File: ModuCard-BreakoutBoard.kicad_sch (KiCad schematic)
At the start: 0 parts

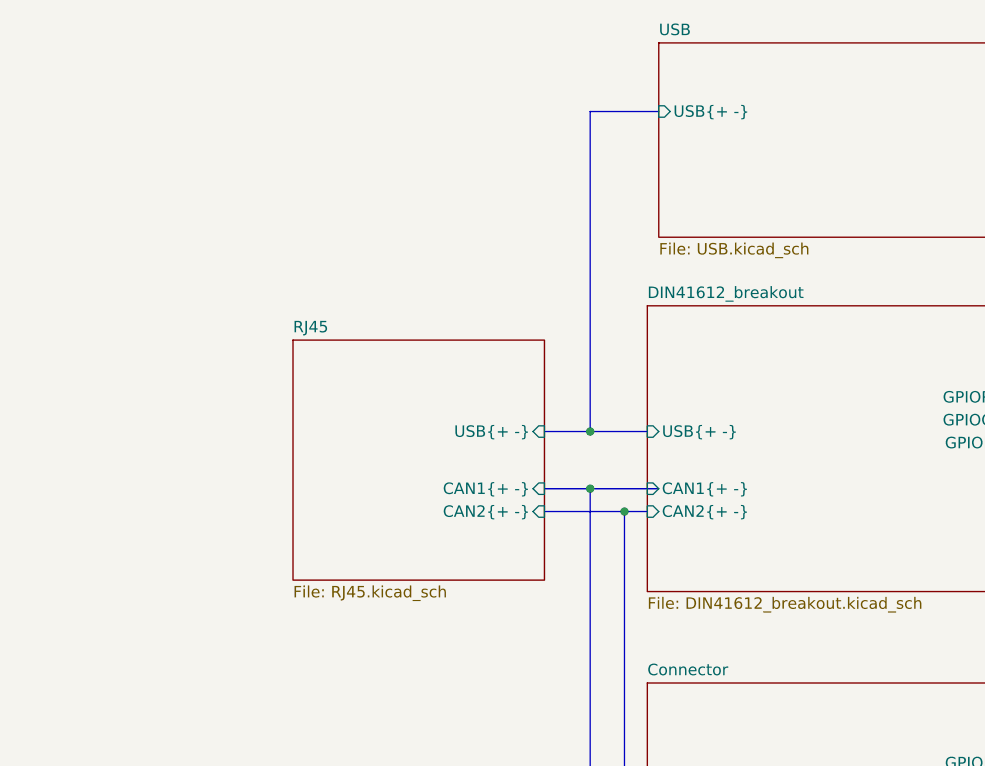
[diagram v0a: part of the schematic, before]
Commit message: Add multiplexer for USB
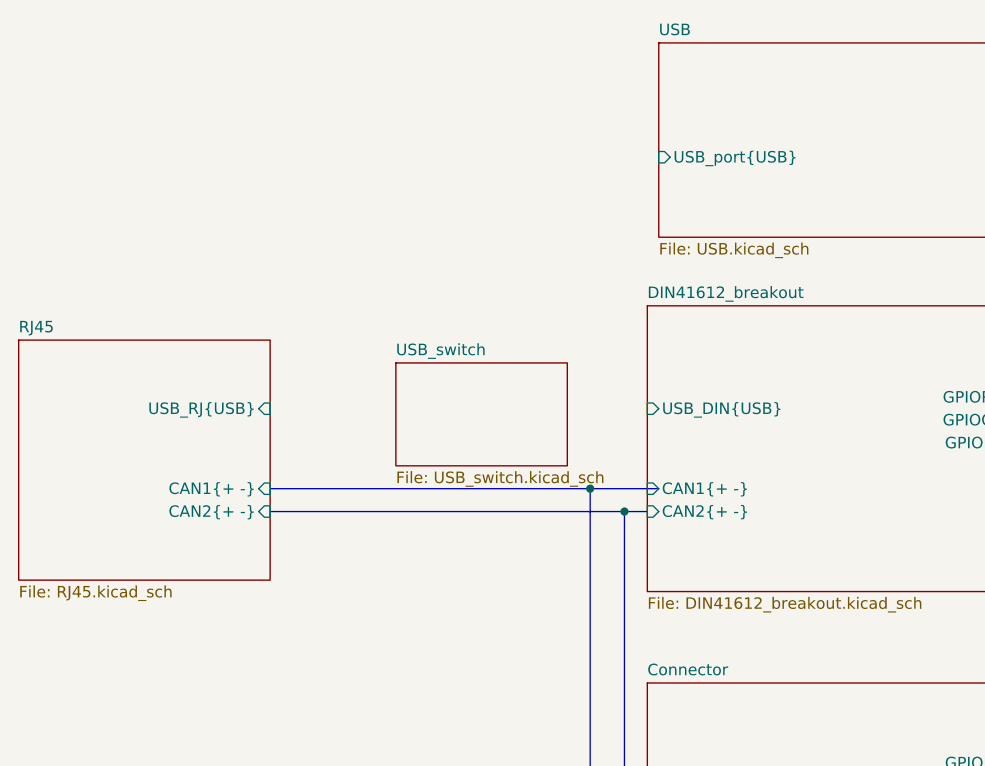
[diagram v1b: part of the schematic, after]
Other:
- added sheet USB_switch (USB_switch.kicad_sch)
- sheet DIN41612_breakout ports: added USB_DIN{USB}; removed USB{+ -}
- sheet RJ45 ports: added USB_RJ{USB}; removed USB{+ -}
- sheet USB ports: added USB_port{USB}; removed USB{+ -}
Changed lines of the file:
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@@
 		(color 0 0 0 0)
 	)
-	(junction
-		(at 111.76 86.36)
-		(diameter 0)
-		(color 0 0 0 0)
-	)
 	(bus
 		(pts
@@
 	(bus
 		(pts
-			(xy 111.76 86.36) (xy 118.11 86.36)
-		)
-		(stroke
-			(width 0)
-			(type default)
-		)
-	)
-	(bus
-		(pts
 			(xy 163.83 128.27) (xy 170.18 128.27)
 		)
@@
 	(bus
 		(pts
-			(xy 106.68 86.36) (xy 111.76 86.36)
-		)
-		(stroke
-			(width 0)
-			(type default)
-		)
-	)
-	(bus
-		(pts
 			(xy 163.83 87.63) (xy 165.1 87.63)
 		)
@@
 	(bus
 		(pts
-			(xy 119.38 50.8) (xy 111.76 50.8)
-		)
-		(stroke
-			(width 0)
-			(type default)
-		)
-	)
-	(bus
-		(pts
-			(xy 106.68 92.71) (xy 111.76 92.71)
-		)
-		(stroke
-			(width 0)
-			(type default)
-		)
-	)
-	(bus
-		(pts
-			(xy 106.68 95.25) (xy 115.57 95.25)
+			(xy 76.2 92.71) (xy 111.76 92.71)
+		)
+		(stroke
+			(width 0)
+			(type default)
+		)
+	)
+	(bus
+		(pts
+			(xy 76.2 95.25) (xy 115.57 95.25)
 		)
 		(stroke
@@
 		(pts
 			(xy 167.64 85.09) (xy 163.83 85.09)
-		)
-		(stroke
-			(width 0)
-			(type default)
-		)
-	)
-	(bus
-		(pts
-			(xy 111.76 50.8) (xy 111.76 86.36)
 		)
 		(stroke
@@
 			)
 		)
-		(pin "USB{+ -}" input
-			(at 118.11 86.36 180)
-			(effects
-				(font
-					(size 1.27 1.27)
-				)
-				(justify left)
-			)
-		)
 		(pin "CAN2{+ -}" input
 			(at 118.11 95.25 180)
@@
 		(pin "CAN1{+ -}" input
 			(at 118.11 92.71 180)
+			(effects
+				(font
+					(size 1.27 1.27)
+				)
+				(justify left)
+			)
+		)
+		(pin "USB_DIN{USB}" input
+			(at 118.11 83.82 180)
 			(effects
 				(font
@@
 			)
 		)
-		(pin "USB{+ -}" input
-			(at 119.38 50.8 180)
+		(pin "USB_port{USB}" input
+			(at 119.38 55.88 180)
 			(effects
 				(font
@@
 	)
 	(sheet
-		(at 78.74 76.2)
+		(at 48.26 76.2)
 		(size 27.94 26.67)
 		(fields_autoplaced yes)
@@
 		)
 		(property "Sheetname" "RJ45"
-			(at 78.74 75.4884 0)
+			(at 48.26 75.4884 0)
 			(effects
 				(font
@@
 		)
 		(property "Sheetfile" "RJ45.kicad_sch"
-			(at 78.74 103.4546 0)
+			(at 48.26 103.4546 0)
 			(effects
 				(font
@@
 			)
 		)
-		(pin "USB{+ -}" input
-			(at 106.68 86.36 0)
-			(effects
-				(font
-					(size 1.27 1.27)
-				)
-				(justify right)
-			)
-		)
 		(pin "CAN2{+ -}" input
-			(at 106.68 95.25 0)
+			(at 76.2 95.25 0)
 			(effects
 				(font
@@
 		)
 		(pin "CAN1{+ -}" input
-			(at 106.68 92.71 0)
+			(at 76.2 92.71 0)
+			(effects
+				(font
+					(size 1.27 1.27)
+				)
+				(justify right)
+			)
+		)
+		(pin "USB_RJ{USB}" input
+			(at 76.2 83.82 0)
 			(effects
 				(font
@@
 				)
 			)
+		)
+	)
+	(sheet
+		(at 90.17 78.74)
+		(size 19.05 11.43)
+		(fields_autoplaced yes)
+		(stroke
+			(width 0.1524)
+			(type solid)
+		)
+		(fill
+			(color 0 0 0 0.0000)
+		)
+		(property "Sheetname" "USB_switch"
+			(at 90.17 78.0284 0)
+			(effects
+				(font
+					(size 1.27 1.27)
+				)
+				(justify left bottom)
+			)
+		)
+		(property "Sheetfile" "USB_switch.kicad_sch"
+			(at 90.17 90.7546 0)
+			(effects
+				(font
+					(size 1.27 1.27)
+				)
+				(justify left top)
+			)
+		)
+		(instances
+			(project "ModuCard-BreakoutBoard"
+				(path "/31ac04e5-0b29-4cf4-90ae-9d7058f5ad37"
+					(page "8")
+				)
+			)

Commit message: Fix USB connection
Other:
- sheet DIN41612_breakout ports: added USB_DIN{+ -}; removed USB_DIN{USB}
- sheet RJ45 ports: added USB_RJ{+ -}; removed USB_RJ{USB}
- sheet USB ports: added USB_port{+ -}, VBUS_IN; removed USB_port{USB}
- sheet USB_switch ports: added USB_DIN{+ -}, USB_RJ{+ -}, USB_port{+ -}, VBUS_IN; removed none
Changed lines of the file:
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@@
 	(paper "A4")
 	(junction
-		(at 111.76 92.71)
+		(at 115.57 97.79)
 		(diameter 0)
 		(color 0 0 0 0)
 	)
 	(junction
-		(at 115.57 95.25)
+		(at 111.76 95.25)
 		(diameter 0)
 		(color 0 0 0 0)
@@
 	(bus
 		(pts
-			(xy 115.57 124.46) (xy 115.57 95.25)
-		)
-		(stroke
-			(width 0)
-			(type default)
-		)
-	)
-	(bus
-		(pts
-			(xy 115.57 95.25) (xy 118.11 95.25)
+			(xy 109.22 87.63) (xy 118.11 87.63)
+		)
+		(stroke
+			(width 0)
+			(type default)
+		)
+	)
+	(bus
+		(pts
+			(xy 76.2 97.79) (xy 115.57 97.79)
+		)
+		(stroke
+			(width 0)
+			(type default)
+		)
+	)
+	(bus
+		(pts
+			(xy 115.57 97.79) (xy 115.57 124.46)
 		)
 		(stroke
@@
 	(bus
 		(pts
+			(xy 109.22 80.01) (xy 114.3 80.01)
+		)
+		(stroke
+			(width 0)
+			(type default)
+		)
+	)
+	(bus
+		(pts
 			(xy 163.83 125.73) (xy 167.64 125.73)
 		)
@@
 		)
 	)
+	(wire
+		(pts
+			(xy 110.49 50.8) (xy 119.38 50.8)
+		)
+		(stroke
+			(width 0)
+			(type default)
+		)
+	)
+	(wire
+		(pts
+			(xy 110.49 74.93) (xy 110.49 50.8)
+		)
+		(stroke
+			(width 0)
+			(type default)
+		)
+	)
 	(bus
 		(pts
@@
 		)
 	)
+	(wire
+		(pts
+			(xy 109.22 74.93) (xy 110.49 74.93)
+		)
+		(stroke
+			(width 0)
+			(type default)
+		)
+	)
 	(bus
 		(pts
@@
 	(bus
 		(pts
-			(xy 111.76 127) (xy 111.76 92.71)
-		)
-		(stroke
-			(width 0)
-			(type default)
-		)
-	)
-	(bus
-		(pts
-			(xy 76.2 92.71) (xy 111.76 92.71)
-		)
-		(stroke
-			(width 0)
-			(type default)
-		)
-	)
-	(bus
-		(pts
-			(xy 76.2 95.25) (xy 115.57 95.25)
+			(xy 111.76 127) (xy 111.76 95.25)
+		)
+		(stroke
+			(width 0)
+			(type default)
+		)
+	)
+	(bus
+		(pts
+			(xy 114.3 55.88) (xy 119.38 55.88)
+		)
+		(stroke
+			(width 0)
+			(type default)
+		)
+	)
+	(bus
+		(pts
+			(xy 114.3 80.01) (xy 114.3 55.88)
+		)
+		(stroke
+			(width 0)
+			(type default)
+		)
+	)
+	(bus
+		(pts
+			(xy 111.76 95.25) (xy 118.11 95.25)
+		)
+		(stroke
+			(width 0)
+			(type default)
+		)
+	)
+	(bus
+		(pts
+			(xy 76.2 95.25) (xy 111.76 95.25)
+		)
+		(stroke
+			(width 0)
+			(type default)
+		)
+	)
+	(bus
+		(pts
+			(xy 76.2 83.82) (xy 90.17 83.82)
 		)
 		(stroke
@@
 	(bus
 		(pts
-			(xy 111.76 92.71) (xy 119.38 92.71)
+			(xy 115.57 97.79) (xy 118.11 97.79)
 		)
 		(stroke
@@
 		)
 		(pin "CAN2{+ -}" input
+			(at 118.11 97.79 180)
+			(effects
+				(font
+					(size 1.27 1.27)
+				)
+				(justify left)
+			)
+		)
+		(pin "CAN1{+ -}" input
 			(at 118.11 95.25 180)
 			(effects
@@
 			)
 		)
-		(pin "CAN1{+ -}" input
-			(at 118.11 92.71 180)
-			(effects
-				(font
-					(size 1.27 1.27)
-				)
-				(justify left)
-			)
-		)
-		(pin "USB_DIN{USB}" input
-			(at 118.11 83.82 180)
+		(pin "USB_DIN{+ -}" input
+			(at 118.11 87.63 180)
 			(effects
 				(font
@@
 			)
 		)
-		(pin "USB_port{USB}" input
+		(pin "USB_port{+ -}" input
 			(at 119.38 55.88 180)
+			(effects
+				(font
+					(size 1.27 1.27)
+				)
+				(justify left)
+			)
+		)
+		(pin "VBUS_IN" input
+			(at 119.38 50.8 180)
 			(effects
 				(font
@@
 		)
 		(pin "CAN2{+ -}" input
+			(at 76.2 97.79 0)
+			(effects
+				(font
+					(size 1.27 1.27)
+				)
+				(justify right)
+			)
+		)
+		(pin "CAN1{+ -}" input
 			(at 76.2 95.25 0)
 			(effects
@@
 			)
 		)
-		(pin "CAN1{+ -}" input
-			(at 76.2 92.71 0)
-			(effects
-				(font
-					(size 1.27 1.27)
-				)
-				(justify right)
-			)
-		)
-		(pin "USB_RJ{USB}" input
+		(pin "USB_RJ{+ -}" input
 			(at 76.2 83.82 0)
 			(effects
@@
 	)
 	(sheet
-		(at 90.17 78.74)
-		(size 19.05 11.43)
+		(at 90.17 71.12)
+		(size 19.05 19.05)
 		(fields_autoplaced yes)
 		(stroke
@@
 		)
 		(property "Sheetname" "USB_switch"
-			(at 90.17 78.0284 0)
+			(at 90.17 70.4084 0)
 			(effects
 				(font
@@
 			)
 		)
+		(pin "USB_DIN{+ -}" input
+			(at 109.22 87.63 0)
+			(effects
+				(font
+					(size 1.27 1.27)
+				)
+				(justify right)
+			)
+		)
+		(pin "USB_port{+ -}" input
+			(at 109.22 80.01 0)
+			(effects
+				(font
+					(size 1.27 1.27)
+				)
+				(justify right)
+			)
+		)
+		(pin "USB_RJ{+ -}" input
+			(at 90.17 83.82 180)
+			(effects
+				(font
+					(size 1.27 1.27)
+				)
+				(justify left)
+			)
+		)
+		(pin "VBUS_IN" input
+			(at 109.22 74.93 0)
+			(effects
+				(font
+					(size 1.27 1.27)
+				)
+				(justify right)
+			)
+		)

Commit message: Add mounting holes
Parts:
- added H1, H2, H3, H4: MountingHole, MountingHole:MountingHole_2.7mm_M2.5_DIN965_Pad, symbol Mechanical:MountingHole_Pad
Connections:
- new net GND: H1.1, H2.1, H3.1, H4.1
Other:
- removed sheet Mounting holes
- note added: "Mounting holes"
